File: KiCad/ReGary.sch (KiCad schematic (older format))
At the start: 10 parts, among them U4 SN74CBT16210, U5 SN74CBT16210, U6 SN74CBT16210, U7 SN74CBT16210, U8 PLCC_84_plug, U9 PLCC_84_plug

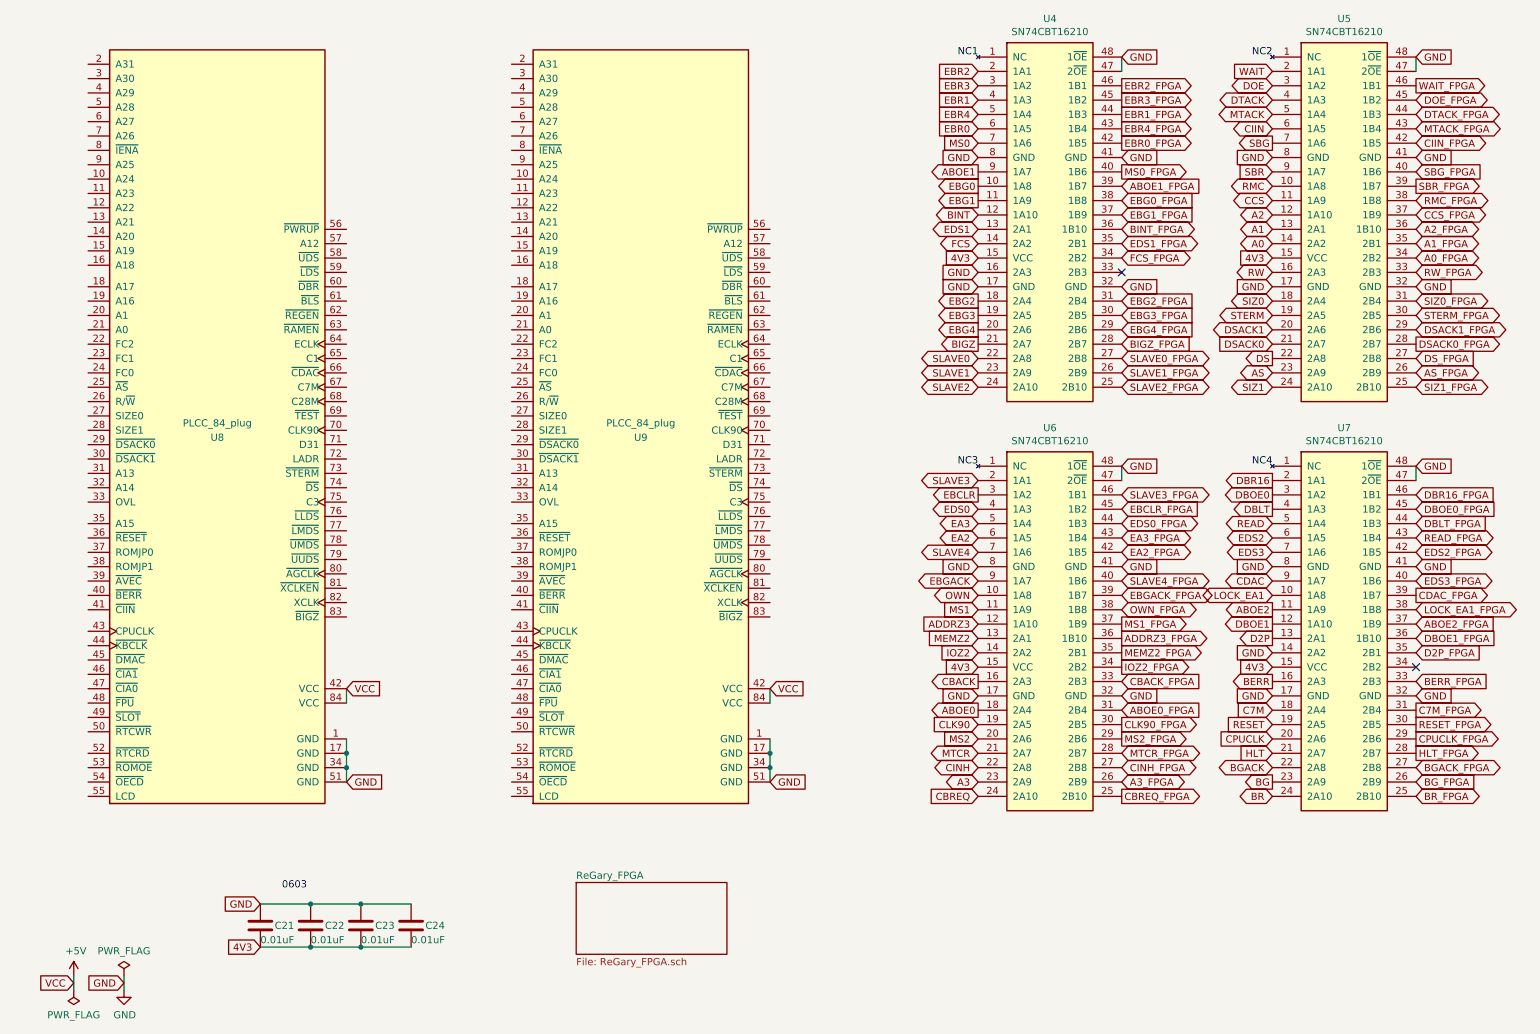
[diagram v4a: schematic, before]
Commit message: Add JP header for JTAGSEL_N, fixed JTAG as dual-purpose pins
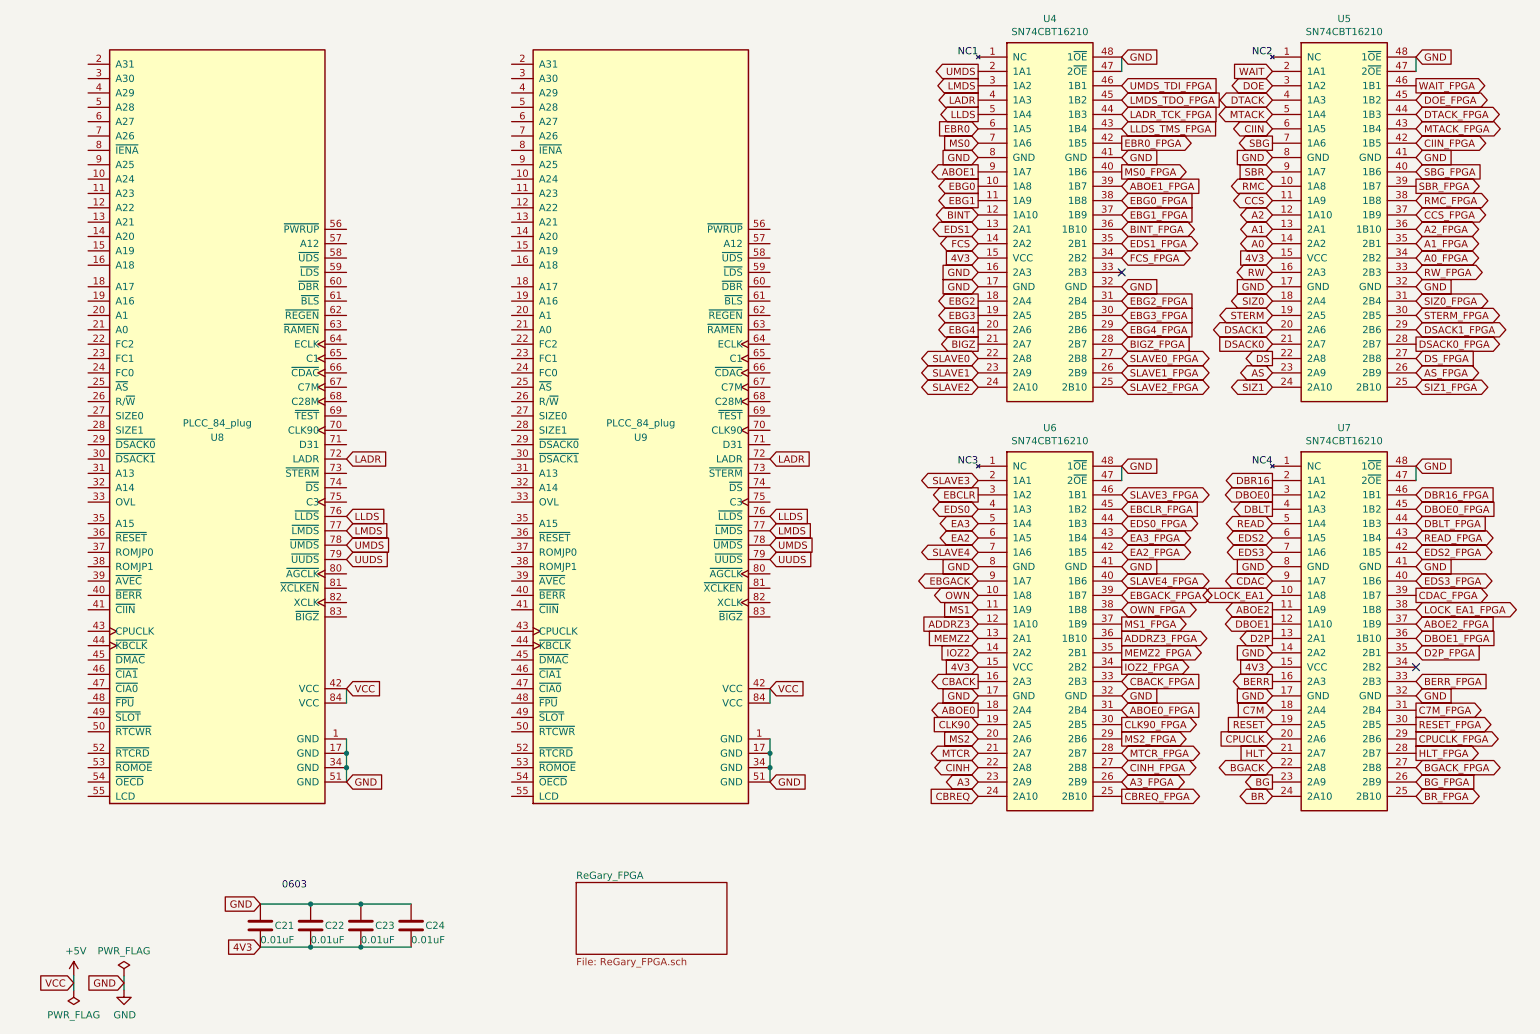
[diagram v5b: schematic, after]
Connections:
- net EBR1 is gone; now on net LADR: U4.4 (1A3)
- net EBR2 is gone; now on net UMDS: U4.2 (1A1)
- net EBR3 is gone; now on net LMDS: U4.3 (1A2)
- net EBR4 is gone; now on net LLDS: U4.5 (1A4)
- net LADR: now reaches U9.72 (LADR)
- net LADR: now also U8.72 (LADR)
- net LLDS: now reaches U9.76 (~LLDS)
- net LLDS: now also U8.76 (~LLDS)
- net LMDS: now reaches U9.77 (~LMDS)
- net LMDS: now also U8.77 (~LMDS)
- net UMDS: now reaches U9.78 (~UMDS)
- net UMDS: now also U8.78 (~UMDS)
- net UUDS: now reaches U9.79 (~UUDS)
- net UUDS: now also U8.79 (~UUDS)
- net EBR1_FPGA renamed LADR_TCK_FPGA
- net EBR2_FPGA renamed UMDS_TDI_FPGA
- net EBR3_FPGA renamed LMDS_TDO_FPGA
- net EBR4_FPGA renamed LLDS_TMS_FPGA
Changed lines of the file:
@@
 Text GLabel 10200 3250 2    50   BiDi ~ 0
 SIZ1_FPGA
-Text GLabel 8150 1450 2    50   Output ~ 0
-EBR4_FPGA
 Text GLabel 8150 1750 2    50   Output ~ 0
 MS0_FPGA
@@
 Text GLabel 8150 1850 2    50   Input ~ 0
 ABOE1_FPGA
-Text GLabel 8150 1350 2    50   Output ~ 0
-EBR1_FPGA
-Text GLabel 8150 1150 2    50   Output ~ 0
-EBR2_FPGA
-Text GLabel 8150 1250 2    50   Output ~ 0
-EBR3_FPGA
 Text GLabel 2750 5350 2    50   Input ~ 0
 VCC
@@
 Text GLabel 7150 1450 0    50   Input ~ 0
 EBR0
-Text GLabel 7150 1250 0    50   Input ~ 0
-EBR1
-Text GLabel 7150 1050 0    50   Input ~ 0
-EBR2
-Text GLabel 7150 1150 0    50   Input ~ 0
-EBR3
-Text GLabel 7150 1350 0    50   Input ~ 0
-EBR4
 Text GLabel 7150 1750 0    50   Output ~ 0
 ABOE1
@@
 Text GLabel 2150 7150 0    50   Input ~ 0
 4V3
+Text GLabel 2750 4350 2    50   Input ~ 0
+UMDS
+Text GLabel 5700 4350 2    50   Input ~ 0
+UMDS
+Text GLabel 7150 1050 0    50   Output ~ 0
+UMDS
+Text GLabel 8150 1150 2    50   Input ~ 0
+UMDS_TDI_FPGA
+Text GLabel 2750 4250 2    50   Input ~ 0
+LMDS
+Text GLabel 5700 4250 2    50   Input ~ 0
+LMDS
+Text GLabel 7150 1150 0    50   Output ~ 0
+LMDS
+Text GLabel 8150 1250 2    50   Input ~ 0
+LMDS_TDO_FPGA
+Text GLabel 2750 4450 2    50   Input ~ 0
+UUDS
+Text GLabel 5700 4450 2    50   Input ~ 0
+UUDS
+Text GLabel 2750 3750 2    50   Input ~ 0
+LADR
+Text GLabel 5700 3750 2    50   Input ~ 0
+LADR
+Text GLabel 7150 1250 0    50   Output ~ 0
+LADR
+Text GLabel 8150 1350 2    50   Input ~ 0
+LADR_TCK_FPGA
+Text GLabel 2750 4150 2    50   Input ~ 0
+LLDS
+Text GLabel 5700 4150 2    50   Input ~ 0
+LLDS
+Text GLabel 7150 1350 0    50   Output ~ 0
+LLDS
+Text GLabel 8150 1450 2    50   Input ~ 0
+LLDS_TMS_FPGA
 $EndSCHEMATC

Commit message: More signal to pin assignments and routing
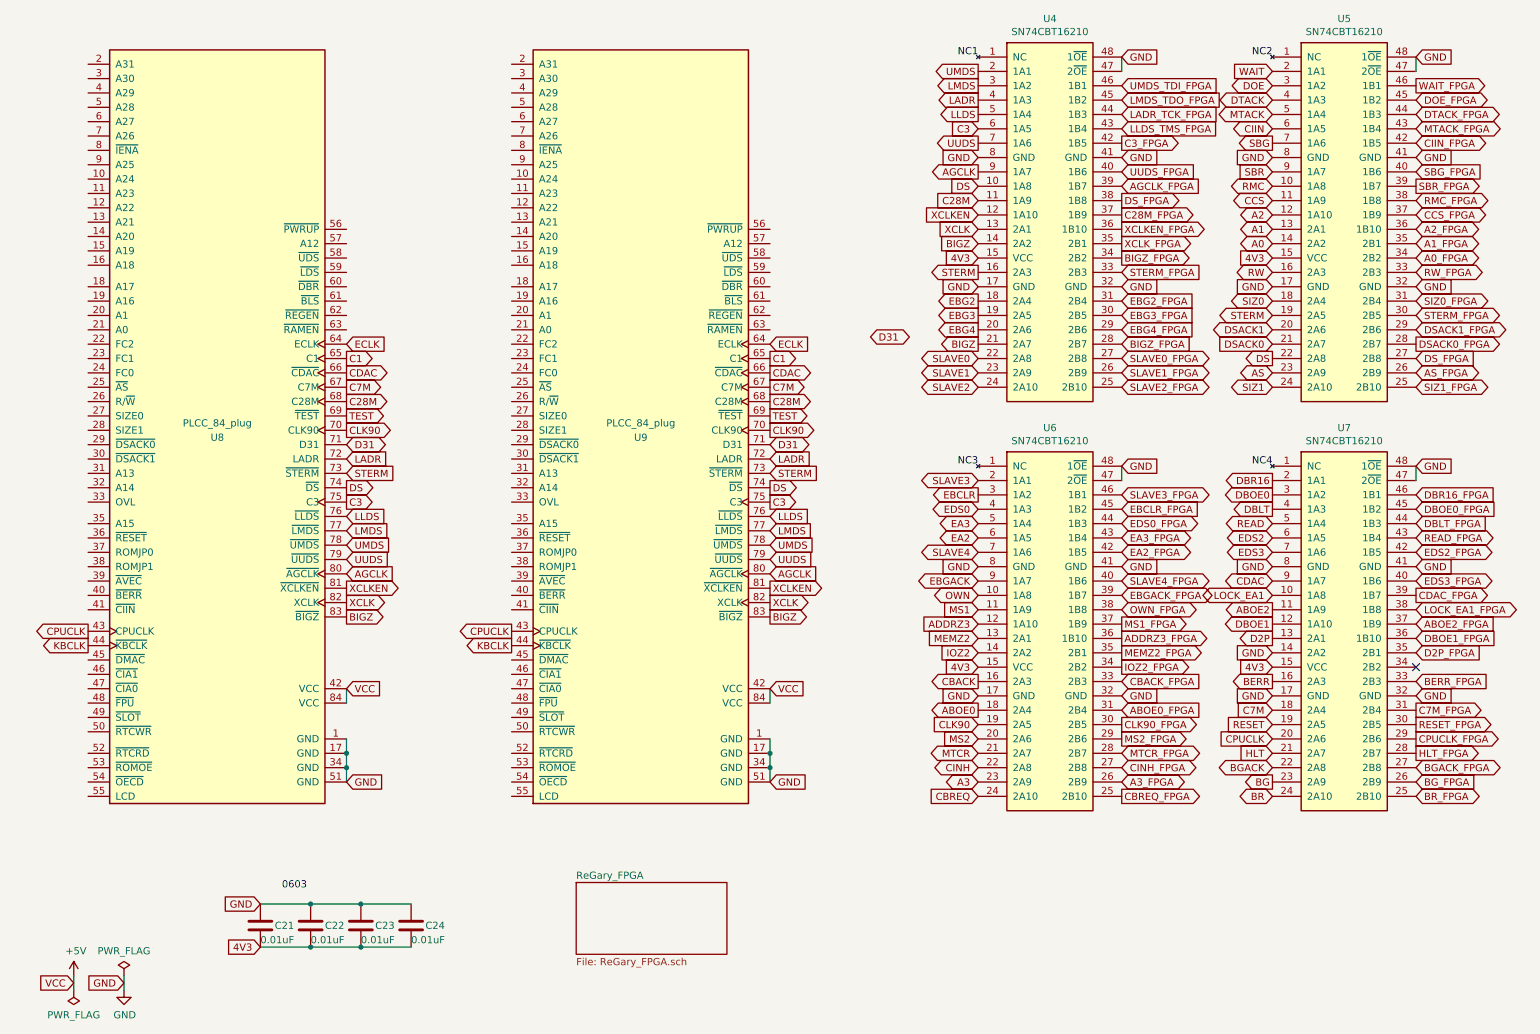
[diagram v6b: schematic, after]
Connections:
- net ABOE1 is gone; now on net AGCLK: U4.9 (1A7)
- net BINT is gone; now on net XCLKEN: U4.12 (1A10)
- net EBG0 is gone; now on net DS: U4.10 (1A8)
- net EBG0_FPGA is gone; now on net DS_FPGA: U4.38 (1B8)
- net EBG1 is gone; now on net C28M: U4.11 (1A9)
- net EBR0 is gone; now on net C3: U4.6 (1A5)
- net EDS1 is gone; now on net XCLK: U4.13 (2A1)
- net FCS is gone; now on net BIGZ: U4.14 (2A2)
- net FCS_FPGA is gone; now on net BIGZ_FPGA: U4.34 (2B2)
- net MS0 is gone; now on net UUDS: U4.7 (1A6)
- net BIGZ: now also U8.83 (~BIGZ), U9.83 (~BIGZ)
- net C7M: now also U8.67 (C7M), U9.67 (C7M)
- net CDAC: now also U8.66 (~CDAC), U9.66 (~CDAC)
- net CLK90: now also U8.70 (CLK90), U9.70 (CLK90)
- net CPUCLK: now also U8.43 (CPUCLK), U9.43 (CPUCLK)
- net DS: now also U8.74 (~DS), U9.74 (~DS)
- net GND: no longer U4.16 (2A3)
- net STERM: now also U4.16 (2A3), U8.73 (~STERM), U9.73 (~STERM)
- net STERM_FPGA: now also U4.33 (2B3)
- net KBCLK: now reaches U9.44 (~KBCLK)
- net KBCLK: now also U8.44 (~KBCLK)
- net ECLK: now reaches U9.64 (ECLK)
- net ECLK: now also U8.64 (ECLK)
- net C1: now reaches U9.65 (C1)
- net C1: now also U8.65 (C1)
- net C28M: now reaches U9.68 (C28M)
- net C28M: now also U8.68 (C28M)
- net TEST: now reaches U9.69 (~TEST)
- net TEST: now also U8.69 (~TEST)
- net D31: now reaches U9.71 (D31)
- net D31: now also U8.71 (D31)
- net C3: now reaches U9.75 (C3)
- net C3: now also U8.75 (C3)
- net AGCLK: now reaches U9.80 (~AGCLK)
- net AGCLK: now also U8.80 (~AGCLK)
- net XCLKEN: now reaches U9.81 (~XCLKEN)
- net XCLKEN: now also U8.81 (~XCLKEN)
- net XCLK: now reaches U9.82 (XCLK)
- net XCLK: now also U8.82 (XCLK)
- net ABOE1_FPGA renamed AGCLK_FPGA
- net BINT_FPGA renamed XCLKEN_FPGA
- net EBG1_FPGA renamed C28M_FPGA
- net EBR0_FPGA renamed C3_FPGA
- net EDS1_FPGA renamed XCLK_FPGA
- net MS0_FPGA renamed UUDS_FPGA
- no-connect marks 2 -> 1
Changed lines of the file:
@@
 Text GLabel 10200 3250 2    50   BiDi ~ 0
 SIZ1_FPGA
-Text GLabel 8150 1750 2    50   Output ~ 0
-MS0_FPGA
-Text GLabel 8150 1950 2    50   Input ~ 0
-EBG0_FPGA
-Text GLabel 8150 2050 2    50   Input ~ 0
-EBG1_FPGA
-Text GLabel 8150 2250 2    50   BiDi ~ 0
-EDS1_FPGA
-Text GLabel 8150 2350 2    50   BiDi ~ 0
-FCS_FPGA
+Text GLabel 8150 1750 2    50   Input ~ 0
+UUDS_FPGA
+Text GLabel 8150 1950 2    50   Output ~ 0
+DS_FPGA
 Text GLabel 8150 2650 2    50   Input ~ 0
 EBG2_FPGA
@@
 	1    0    0    -1
 $EndComp
-Text GLabel 8150 1850 2    50   Input ~ 0
-ABOE1_FPGA
 Text GLabel 2750 5350 2    50   Input ~ 0
 VCC
-Text GLabel 8150 2150 2    50   BiDi ~ 0
-BINT_FPGA
+Text GLabel 8150 2250 2    50   Output ~ 0
+XCLK_FPGA
 Text GLabel 8150 4600 2    50   BiDi ~ 0
 SLAVE4_FPGA
-Text GLabel 7150 2250 0    50   BiDi ~ 0
-FCS
 Text GLabel 9200 1950 0    50   BiDi ~ 0
 CCS
@@
 Text GLabel 7150 4200 0    50   BiDi ~ 0
 EA3
-Text GLabel 7150 2150 0    50   BiDi ~ 0
-EDS1
-Text GLabel 7150 2050 0    50   BiDi ~ 0
-BINT
-Text GLabel 7150 1550 0    50   Input ~ 0
-MS0
-Text GLabel 7150 1450 0    50   Input ~ 0
-EBR0
-Text GLabel 7150 1750 0    50   Output ~ 0
-ABOE1
-Text GLabel 7150 1850 0    50   Output ~ 0
-EBG0
-Text GLabel 7150 1950 0    50   Output ~ 0
-EBG1
 Text GLabel 7150 2650 0    50   Output ~ 0
 EBG2
@@
 Text GLabel 9200 5100 0    50   Input ~ 0
 GND
-Text GLabel 7150 2450 0    50   Input ~ 0
-GND
 Text GLabel 8150 1550 2    50   Output ~ 0
-EBR0_FPGA
-NoConn ~ 8150 2450
+C3_FPGA
 Text GLabel 10200 2350 2    50   BiDi ~ 0
 A0_FPGA
@@
 Text GLabel 8150 1450 2    50   Input ~ 0
 LLDS_TMS_FPGA
+Text GLabel 950  4950 0    50   Output ~ 0
+CPUCLK
+Text GLabel 950  5050 0    50   Output ~ 0
+KBCLK
+Text GLabel 2750 4750 2    50   Output ~ 0
+XCLK
+Text GLabel 5700 4750 2    50   Output ~ 0
+XCLK
+Text GLabel 2750 3550 2    50   Output ~ 0
+CLK90
+Text GLabel 2750 3350 2    50   Output ~ 0
+C28M
+Text GLabel 2750 3250 2    50   Output ~ 0
+C7M
+Text GLabel 2750 3150 2    50   Output ~ 0
+CDAC
+Text GLabel 2750 3050 2    50   Output ~ 0
+C1
+Text GLabel 2750 4050 2    50   Output ~ 0
+C3
+Text GLabel 5700 3550 2    50   Output ~ 0
+CLK90
+Text GLabel 5700 3350 2    50   Output ~ 0
+C28M
+Text GLabel 5700 3250 2    50   Output ~ 0
+C7M
+Text GLabel 5700 3150 2    50   Output ~ 0
+CDAC
+Text GLabel 5700 3050 2    50   Output ~ 0
+C1
+Text GLabel 5700 4050 2    50   Output ~ 0
+C3
+Text GLabel 2750 2950 2    50   Input ~ 0
+ECLK
+Text GLabel 2750 3450 2    50   Output ~ 0
+TEST
+Text GLabel 5700 2950 2    50   Input ~ 0
+ECLK
+Text GLabel 3900 4950 0    50   Output ~ 0
+CPUCLK
+Text GLabel 3900 5050 0    50   Output ~ 0
+KBCLK
+Text GLabel 5700 3450 2    50   Output ~ 0
+TEST
+Text GLabel 2750 4550 2    50   Input ~ 0
+AGCLK
+Text GLabel 5700 4550 2    50   Input ~ 0
+AGCLK
+Text GLabel 5700 3650 2    50   BiDi ~ 0
+D31
+Text GLabel 5700 3850 2    50   Input ~ 0
+STERM
+Text GLabel 5700 3950 2    50   Output ~ 0
+DS
+Text GLabel 2750 3650 2    50   BiDi ~ 0
+D31
+Text GLabel 2750 3850 2    50   Input ~ 0
+STERM
+Text GLabel 2750 3950 2    50   Output ~ 0
+DS
+Text GLabel 2750 4650 2    50   Output ~ 0
+XCLKEN
+Text GLabel 5700 4650 2    50   Output ~ 0
+XCLKEN
+Text GLabel 2750 4850 2    50   Output ~ 0
+BIGZ
+Text GLabel 5700 4850 2    50   Output ~ 0
+BIGZ
+Text GLabel 7150 2150 0    50   Input ~ 0
+XCLK
+Text GLabel 7150 1450 0    50   Input ~ 0
+C3
+Text GLabel 7150 1550 0    50   Output ~ 0
+UUDS
+Text GLabel 8150 1850 2    50   Input ~ 0
+AGCLK_FPGA
+Text GLabel 7150 1750 0    50   Output ~ 0
+AGCLK
+Text GLabel 7150 1850 0    50   Input ~ 0
+DS
+Text GLabel 7150 2050 0    50   Input ~ 0
+XCLKEN
+Text GLabel 8150 2150 2    50   Output ~ 0
+XCLKEN_FPGA
+Text GLabel 7150 2450 0    50   Output ~ 0
+STERM
+Text GLabel 8150 2450 2    50   Input ~ 0
+STERM_FPGA
+Text GLabel 6400 2900 2    50   BiDi ~ 0
+D31
+Text GLabel 8150 2350 2    50   Output ~ 0
+BIGZ_FPGA
+Text GLabel 7150 2250 0    50   Input ~ 0
+BIGZ
+Text GLabel 7150 1950 0    50   Input ~ 0
+C28M
+Text GLabel 8150 2050 2    50   Output ~ 0
+C28M_FPGA
 $EndSCHEMATC
